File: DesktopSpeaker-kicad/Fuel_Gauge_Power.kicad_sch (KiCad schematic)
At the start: 15 parts, among them U12 TPS7A0230PDBVR, U13 TS5A3167DBVR, U16 TS5A3167DBVR, U17 TS5A3167DBVR, U5 MAX17048G+T10

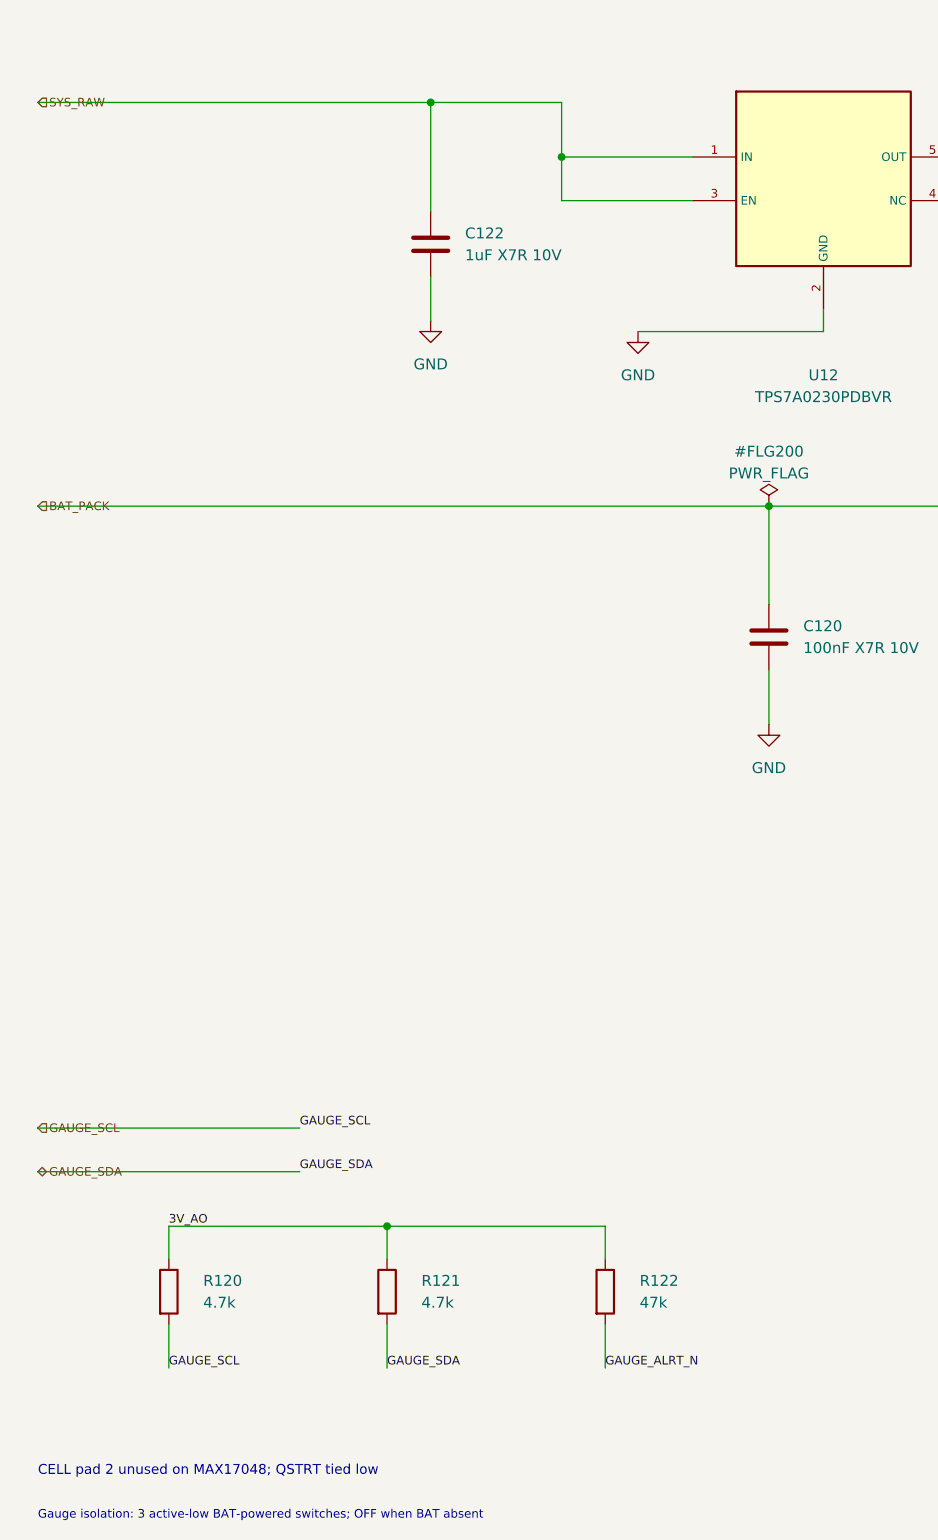
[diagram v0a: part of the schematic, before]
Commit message: Integrate USB auxiliary logic mux and reconcile active BOM
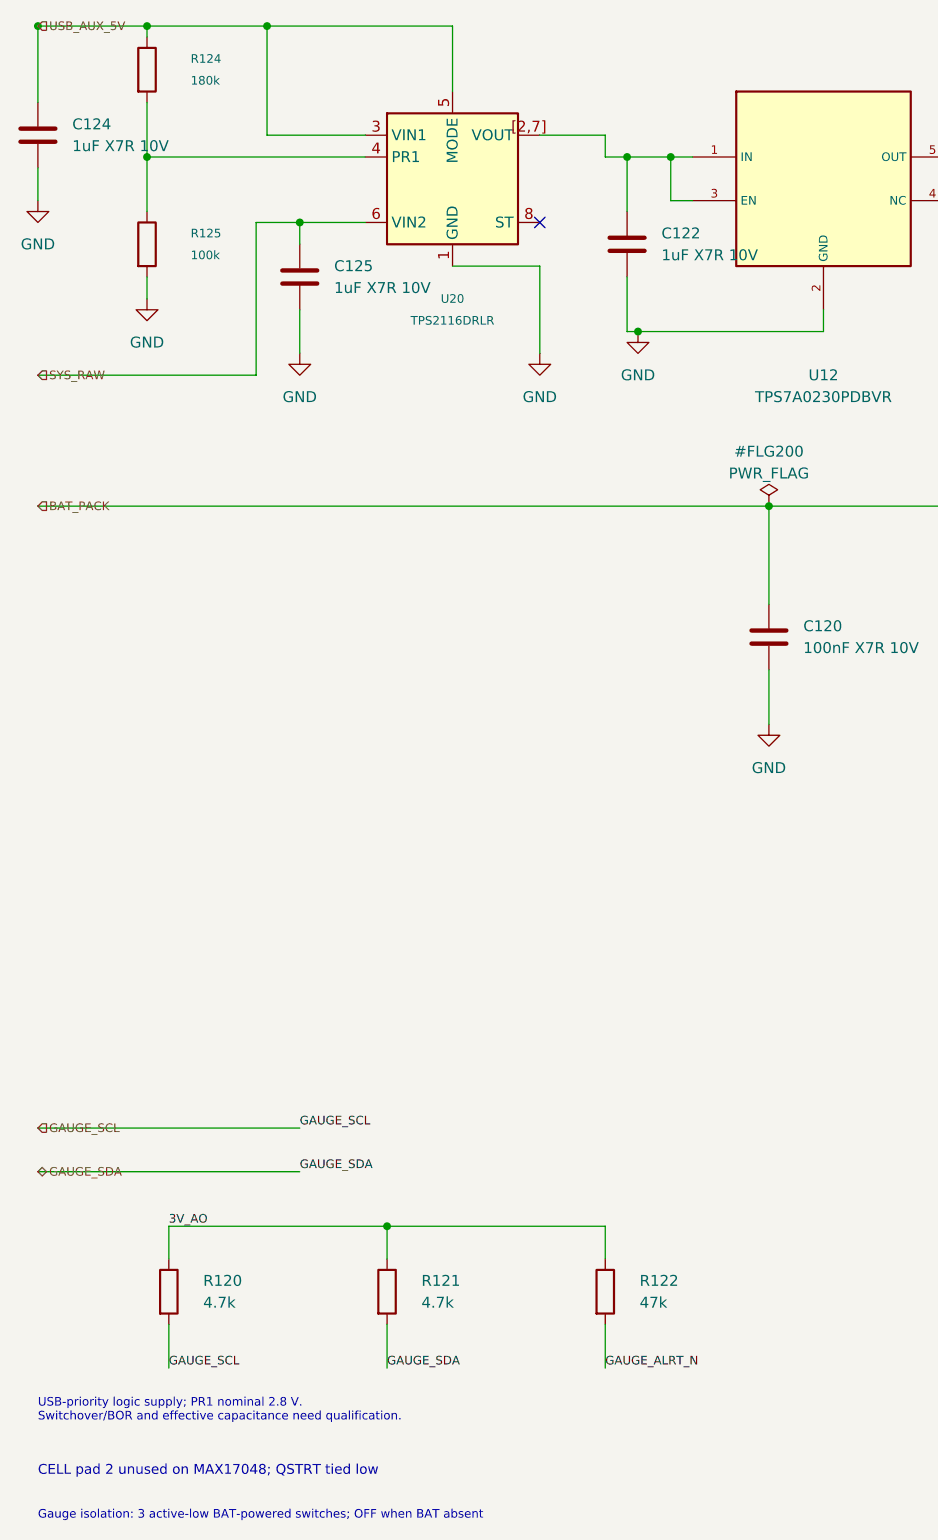
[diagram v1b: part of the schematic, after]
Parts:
- added C124, C125: 1uF X7R 10V, DesktopSpeaker:PD_C_0603, symbol PD_C:PD_C
- added R124: 180k, DesktopSpeaker:PD_R_0603, symbol PD_R:PD_R
- added R125: 100k, DesktopSpeaker:PD_R_0603, symbol PD_R:PD_R
- added U20: TPS2116DRLR, DesktopSpeaker:TPS2116DRLR, symbol TPS2116DRLR:TPS2116DRLR
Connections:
- net GND: now also C124.2, C125.2, R125.2, U20.1 (GND)
- net SYS_RAW: now also C125.1, U20.6 (VIN2); no longer C122.1, U12.1 (IN), U12.3 (EN)
- new net: R124.2, R125.1, U20.4 (PR1)
- new net: C122.1, U12.1 (IN), U12.3 (EN), U20.[2,7] (VOUT)
- new net USB_AUX_5V: C124.1, R124.1, U20.3 (VIN1), U20.5 (MODE)
- no-connect marks 2 -> 3
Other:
- note added: "USB-priority logic supply; PR1 nominal 2.8 V. Switchover/BOR and effective capacitance need qualification."
- moved on the sheet: C122

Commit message: Qualify gauge bus by battery voltage and reconcile supervisor BOM
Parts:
- added C126: 100nF, DesktopSpeaker:PD_C_0603, symbol PD_C:PD_C
- added Q104: 2N7002, DesktopSpeaker:2N7002, symbol 2N7002:2N7002
- added R126, R127: 1M, DesktopSpeaker:PD_R_0603, symbol PD_R:PD_R
- added U21: TPS3839G33DBZR, DesktopSpeaker:TPS3839G33DBZR, symbol TPS3839G33DBZR:TPS3839G33DBZR
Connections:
- net 3V_AO: now also C130.1, C131.1, C132.1, U13.5 (VCC), U16.5 (VCC), U17.5 (VCC), R126.1
- net BAT_PACK: now also C126.1, U21.3 (VDD); no longer C130.1, C131.1, C132.1, U13.5 (VCC), U16.5 (VCC), U17.5 (VCC)
- net GND: now also C126.2, Q104.2 (S), R127.2, U21.1 (GND); no longer U13.4 (IN), U16.4 (IN), U17.4 (IN)
- new net: Q104.1 (G), R127.1, U21.2 (RESET)
- new net GAUGE_ISO_N: Q104.3 (D), R126.2, U13.4 (IN), U16.4 (IN), U17.4 (IN)
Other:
- note added: "Gauge bus: AO-powered switches; default OFF below valid battery. U21 3.08 V supervisor enables Q104 after reset recovery."
- note removed: "Gauge isolation: 3 active-low BAT-powered switches; OFF when BAT absent"
